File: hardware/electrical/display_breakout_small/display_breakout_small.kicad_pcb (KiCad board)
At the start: 2 copper layers, 52 x 62.5 mm, 22 parts, among them J1 Conn_02x10_Odd_Even, J2 Conn_01x14_Socket, Q1 2N7002, SW1 RotaryEncoder_Switch, SW2 SW_Push, SW3 SW_Push

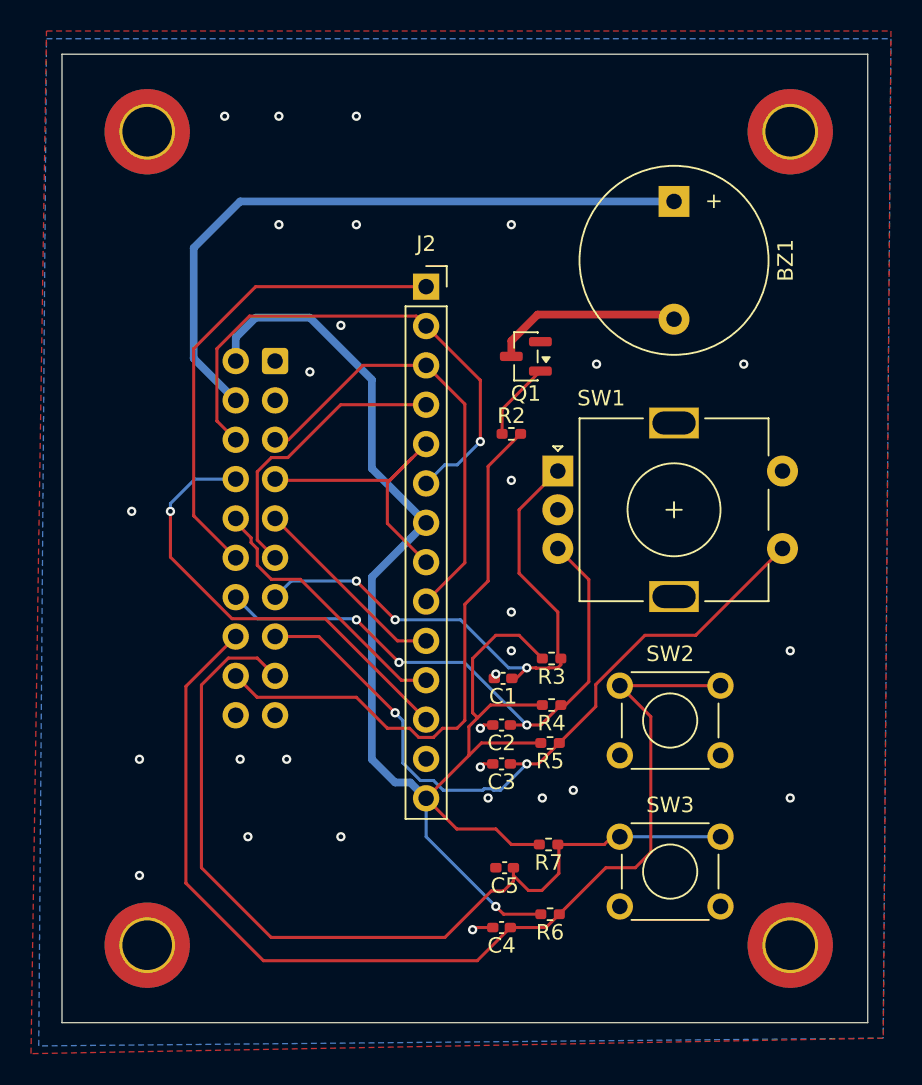
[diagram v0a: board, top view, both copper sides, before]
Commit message: added silkscreen team name and rounded pcb corners
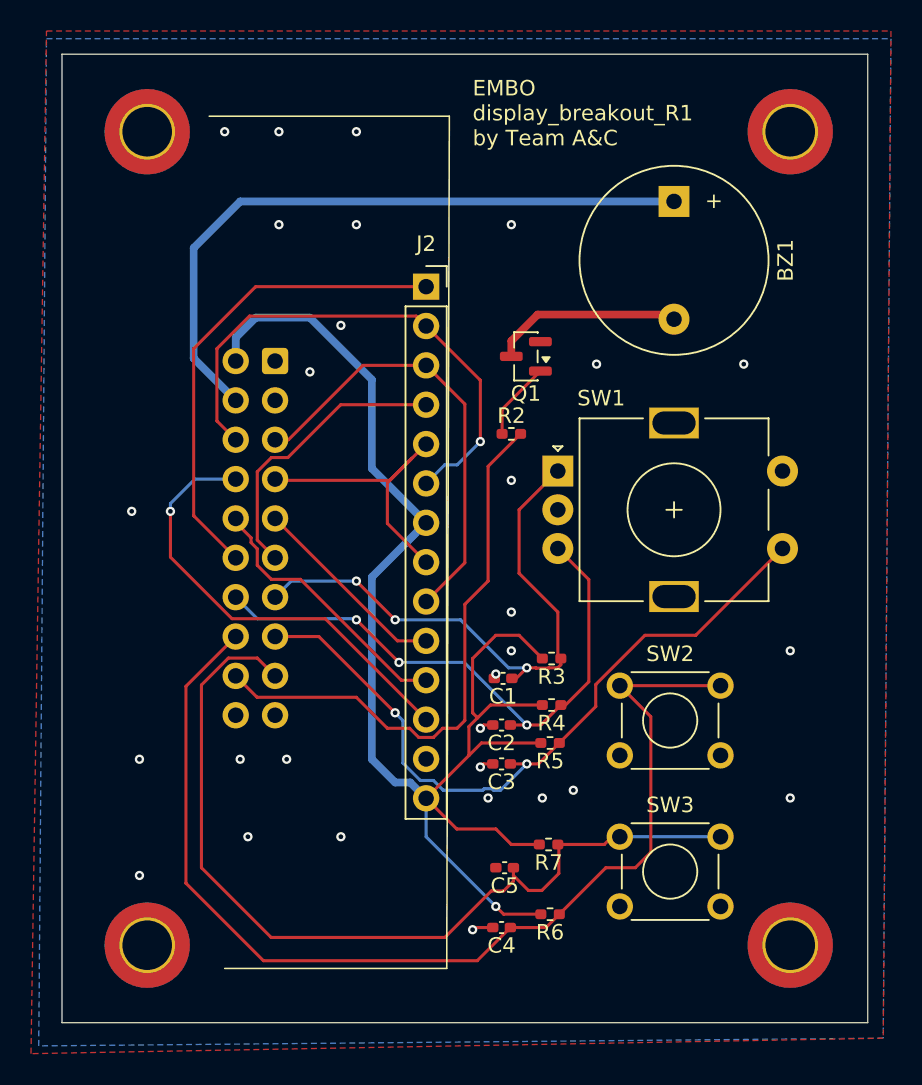
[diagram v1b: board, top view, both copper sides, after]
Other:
- board text added: "EMBO display_breakout_R1 by Team A&C"
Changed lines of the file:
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@@
 		)
+	)
+	(gr_line
+		(start 195.5 57.5)
+		(end 211 57.5)
+		(stroke
+			(width 0.1)
+			(type default)
+		)
+		(layer "F.SilkS")
+	)
+	(gr_line
+		(start 210.83 112.5)
+		(end 196.5 112.5)
+		(stroke
+			(width 0.1)
+			(type default)
+		)
+		(layer "F.SilkS")
+	)
+	(gr_line
+		(start 211 57.5)
+		(end 210.83 112.5)
+		(stroke
+			(width 0.1)
+			(type default)
+		)
+		(layer "F.SilkS")
 	)
 	(gr_rect
@@
 		(start 186 53.5)
 		(end 238 116)
+		(radius 2)
 		(stroke
 			(width 0.05)
-			(type default)
+			(type solid)
 		)
 		(fill no)
 		(layer "Edge.Cuts")
 	)
+	(gr_text "EMBO \ndisplay_breakout_R1\nby Team A&C"
+		(at 212.5 59.5 0)
+		(layer "F.SilkS")
+		(effects
+			(font
+				(size 1 1)
+				(thickness 0.1)
+			)
+			(justify left bottom)
+		)
+	)
 	(segment
 		(start 216.875 73.95)
@@
 	)
 	(via
-		(at 205 57.5)
+		(at 205 58.5)
 		(size 0.6)
 		(drill 0.3)
@@
 	)
 	(via
-		(at 196.5 57.5)
+		(at 196.5 58.5)
 		(size 0.6)
 		(drill 0.3)
@@
 	)
 	(via
-		(at 200 57.5)
-		(size 0.6)
-		(drill 0.3)
+		(at 200 58.5)
+		(size 0.6)
+		(drill 0.3)
